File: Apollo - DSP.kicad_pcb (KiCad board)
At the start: 4 copper layers, 82.9 x 59.1 mm, 72 parts, among them J1 USB_C_Receptacle_USB2.0, J2 Conn_01x04, J3 MEM2067-02-180-00-A_REVB, J4 Conn_01x04, J5 Conn_01x04, J6 Conn_01x04, J7 Conn_01x06, U1 NCP115ASN330T2G, U2 USBLC6-2SC6, U3 NCP115ASN330T2G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

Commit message: minor modifications with refs and new pictures
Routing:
- net GND: track 260.4 -> 261.1 mm, vias 190 -> 269

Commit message: fixed mounting hole size from 6mm diam to 3mm diam
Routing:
- net GND: vias 269 -> 297
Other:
- outline, holes or cut-outs redrawn

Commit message: own foorprint for LDO
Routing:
- net GND: vias 297 -> 285

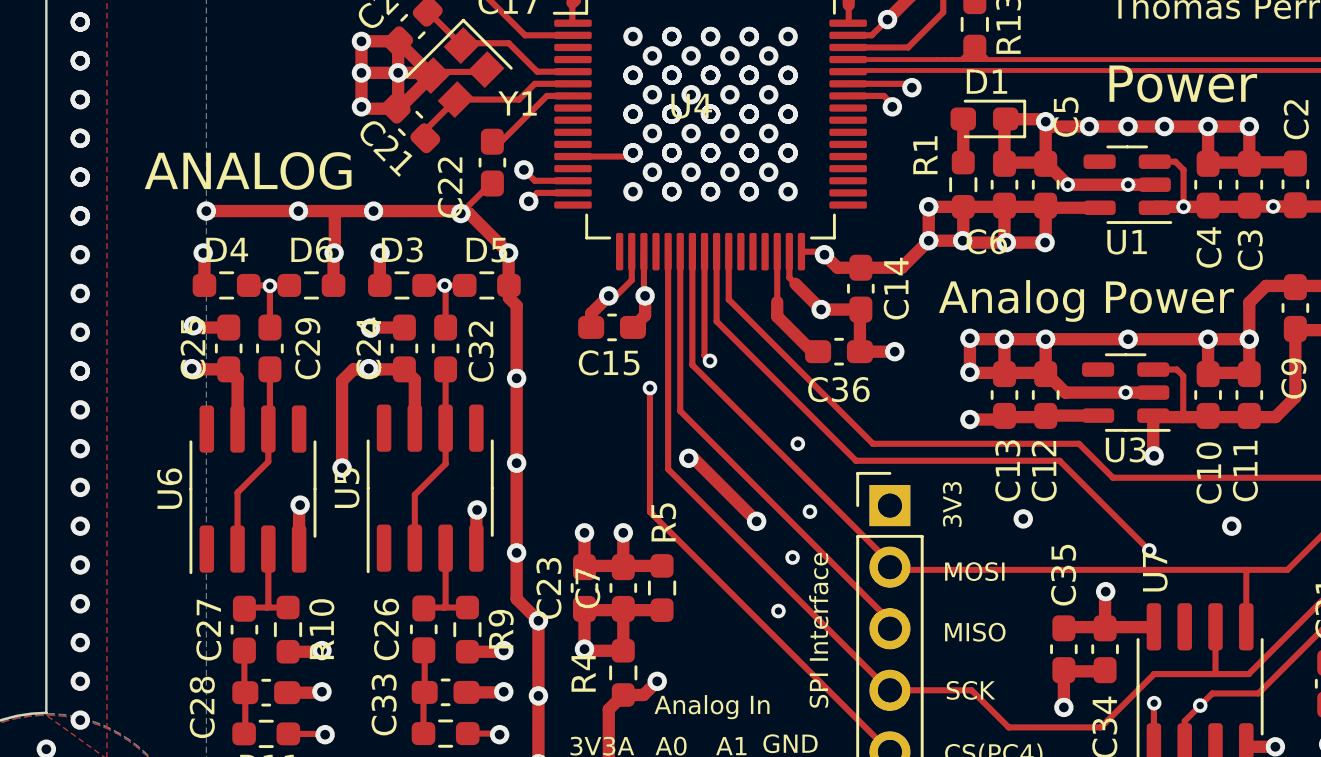
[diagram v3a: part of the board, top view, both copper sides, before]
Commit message: replaced 741 opamp for lm358 due to cost reasons
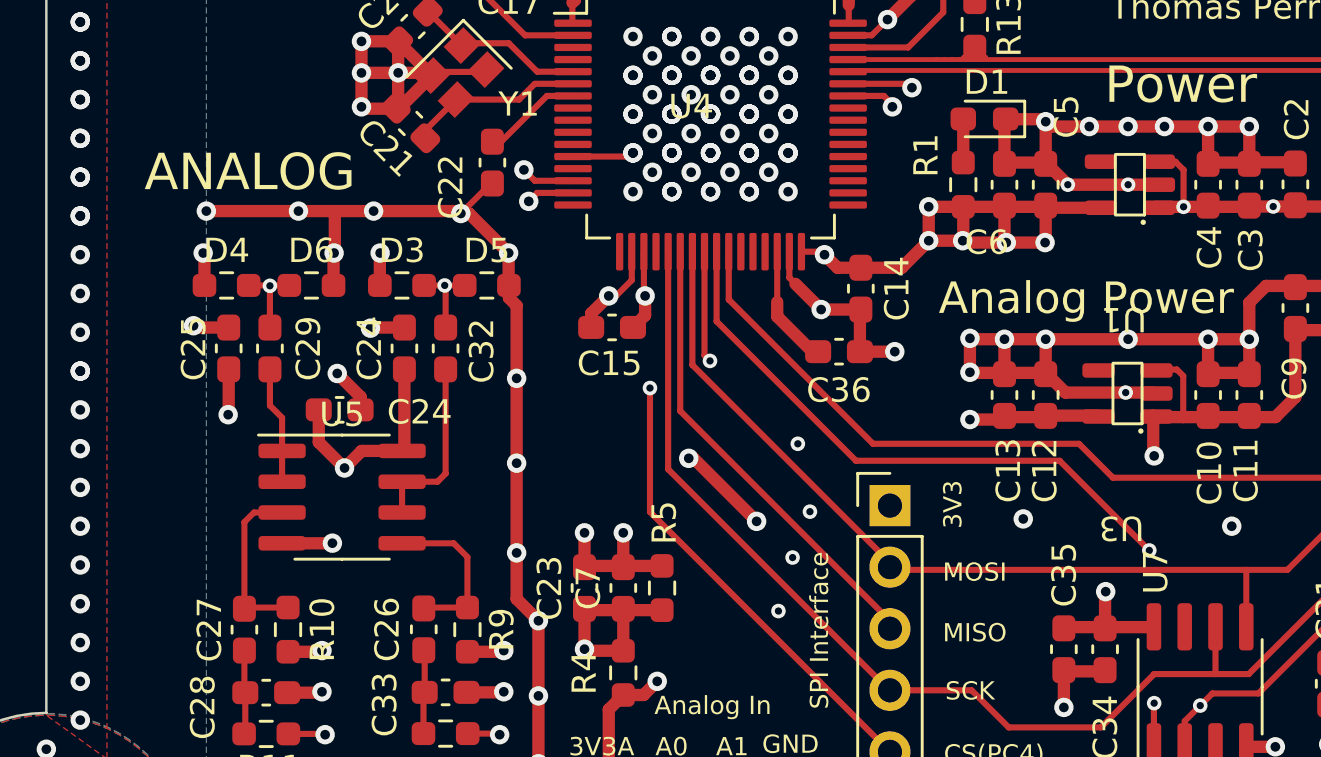
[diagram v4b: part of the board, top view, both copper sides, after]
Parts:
- removed U6: UA741, Package_SO:SOIC-8_3.9x4.9mm_P1.27mm
- added C24: 100n, Capacitor_SMD:C_0603_1608Metric_Pad1.08x0.95mm_HandSolder, F.Cu at (64.0, 106.7)
- U1, U3: footprint Package_TO_SOT_SMD:SOT-23-5 -> NCP115ASN330T2G:NCP115ASN330T2G
- U5: value UA741 -> LM358
- moved U5 3.65 mm to (64.1, 110.3), turned to 0 degrees
- moved U1 0.11 mm to (96.6, 97.4)
- moved U3 0.08 mm to (96.5, 106.0)
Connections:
- U1 pad 4: unconnected-(U1-Pad4) -> (no net)
- U3 pad 4: unconnected-(U3-Pad4) -> (no net)
- U5 pad 1: (no net) -> /Analog/CH0_OP_OUT
- U5 pad 2: /Analog/CH1_OP_OUT -> /Analog/CH0_OP_OUT
- U5 pad 3: /Analog/CH1_+ -> /Analog/CH0_+
- U5 pad 5: (no net) -> /Analog/CH1_+
- U5 pad 7: +5VA -> /Analog/CH1_OP_OUT
- U5 pad 8: unconnected-(U5-Pad8) -> +5VA
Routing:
- net +5VA: track 74.1 -> 68.5 mm, vias 6 -> 5
- net /Analog/CH0_OP_OUT: track 8.03 -> 4.84 mm
- net /Analog/CH0_+: track 4.20 -> 7.11 mm
- net /Analog/CH1_+: track 4.23 -> 6.83 mm

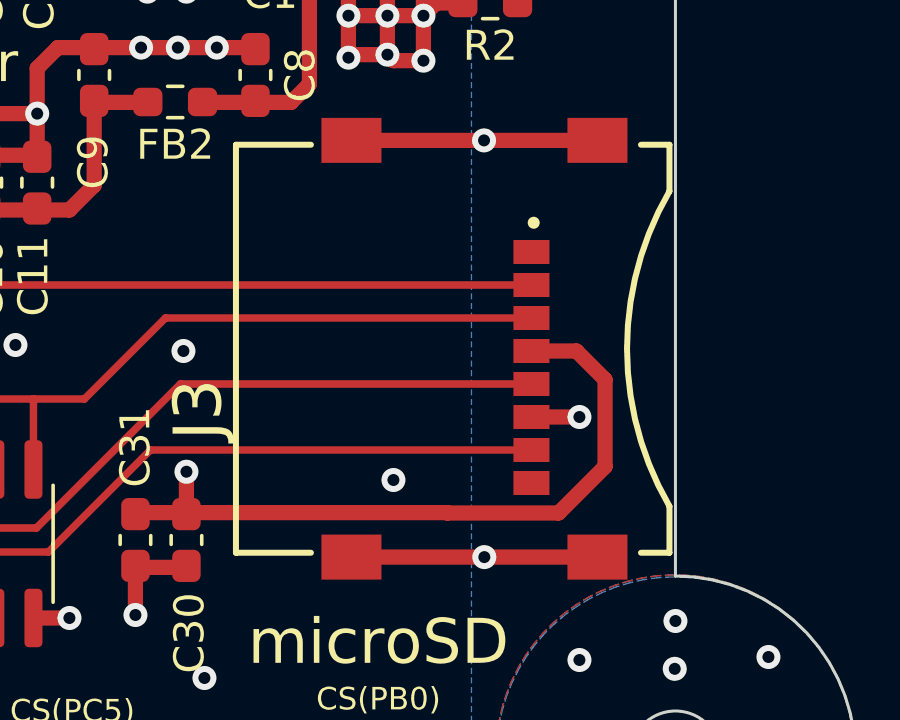
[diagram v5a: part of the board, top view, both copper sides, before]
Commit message: added jlcpcb ordernumber location
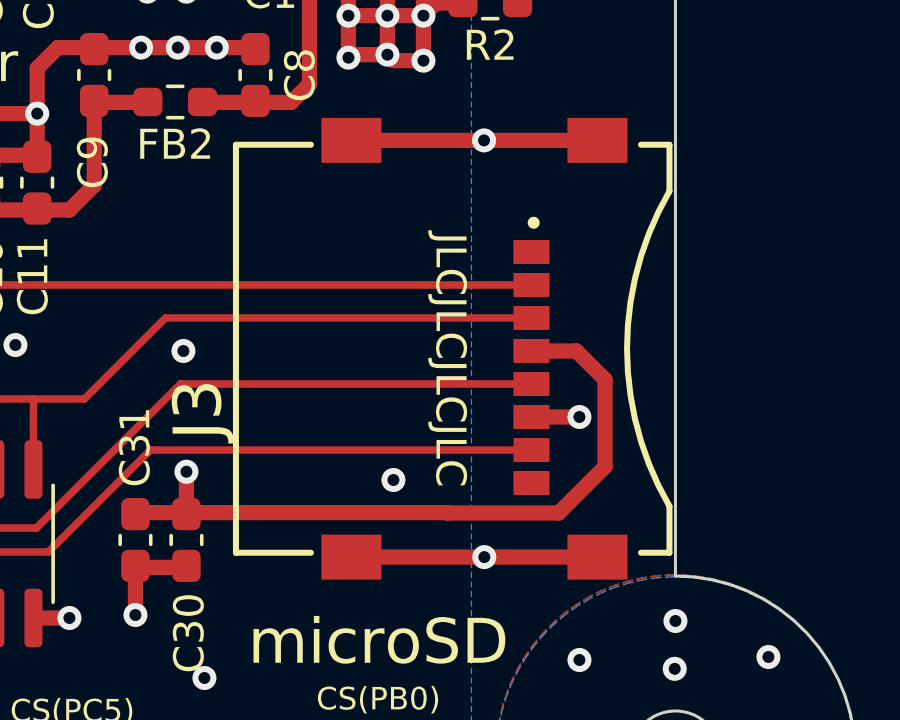
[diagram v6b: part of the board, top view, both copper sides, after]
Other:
- board text added: "JLCJLCJLCJLC"
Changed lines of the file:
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@@
     (effects (font (size 0.75 0.75) (thickness 0.1875)))
+  )
+  (gr_text "JLCJLCJLCJLC" (at 115.3 112 270) (layer "F.SilkS")
+    (effects (font (size 1 1) (thickness 0.15)))
   )
   (gr_text "MOSI" (at 90.2 113.4) (layer "F.SilkS")

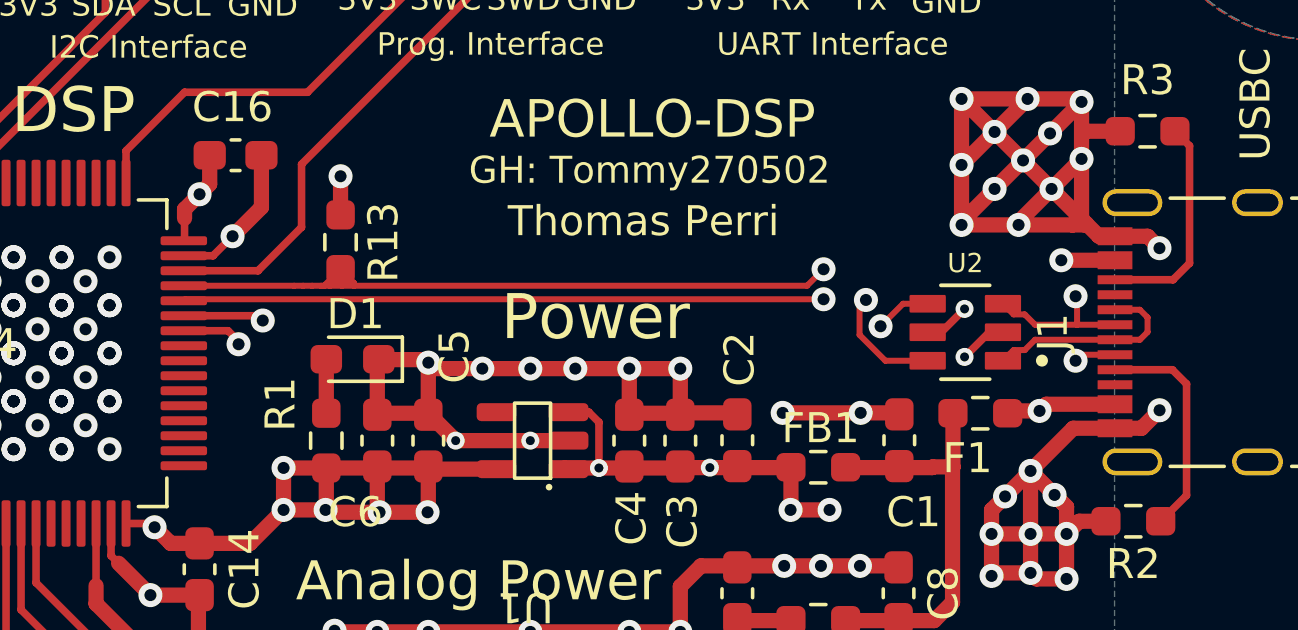
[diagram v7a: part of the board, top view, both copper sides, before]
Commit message: tiedied usb differential pair routing
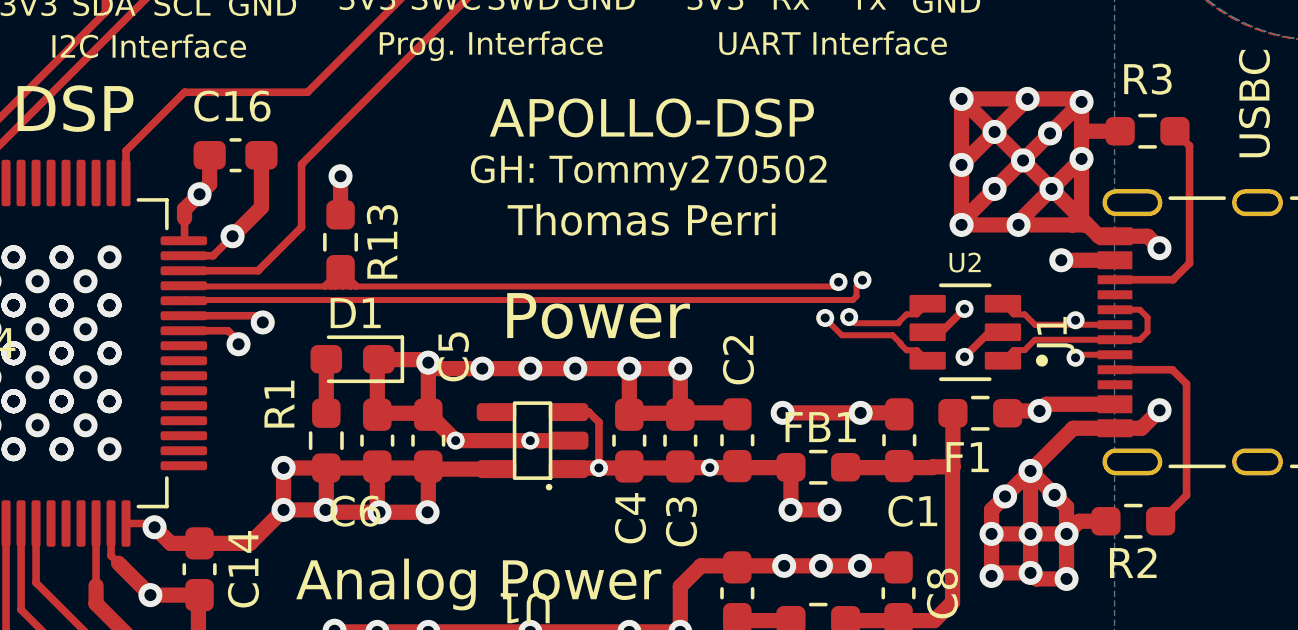
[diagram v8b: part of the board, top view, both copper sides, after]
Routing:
- net USB_D-: track 25.5 -> 27.7 mm
- net USB_CONN_-: track 8.54 -> 6.80 mm
- net USB_D+: track 30.0 -> 31.5 mm
